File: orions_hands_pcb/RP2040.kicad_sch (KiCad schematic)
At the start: 25 parts, among them U1 RP2040, X1 ASE-12MHz

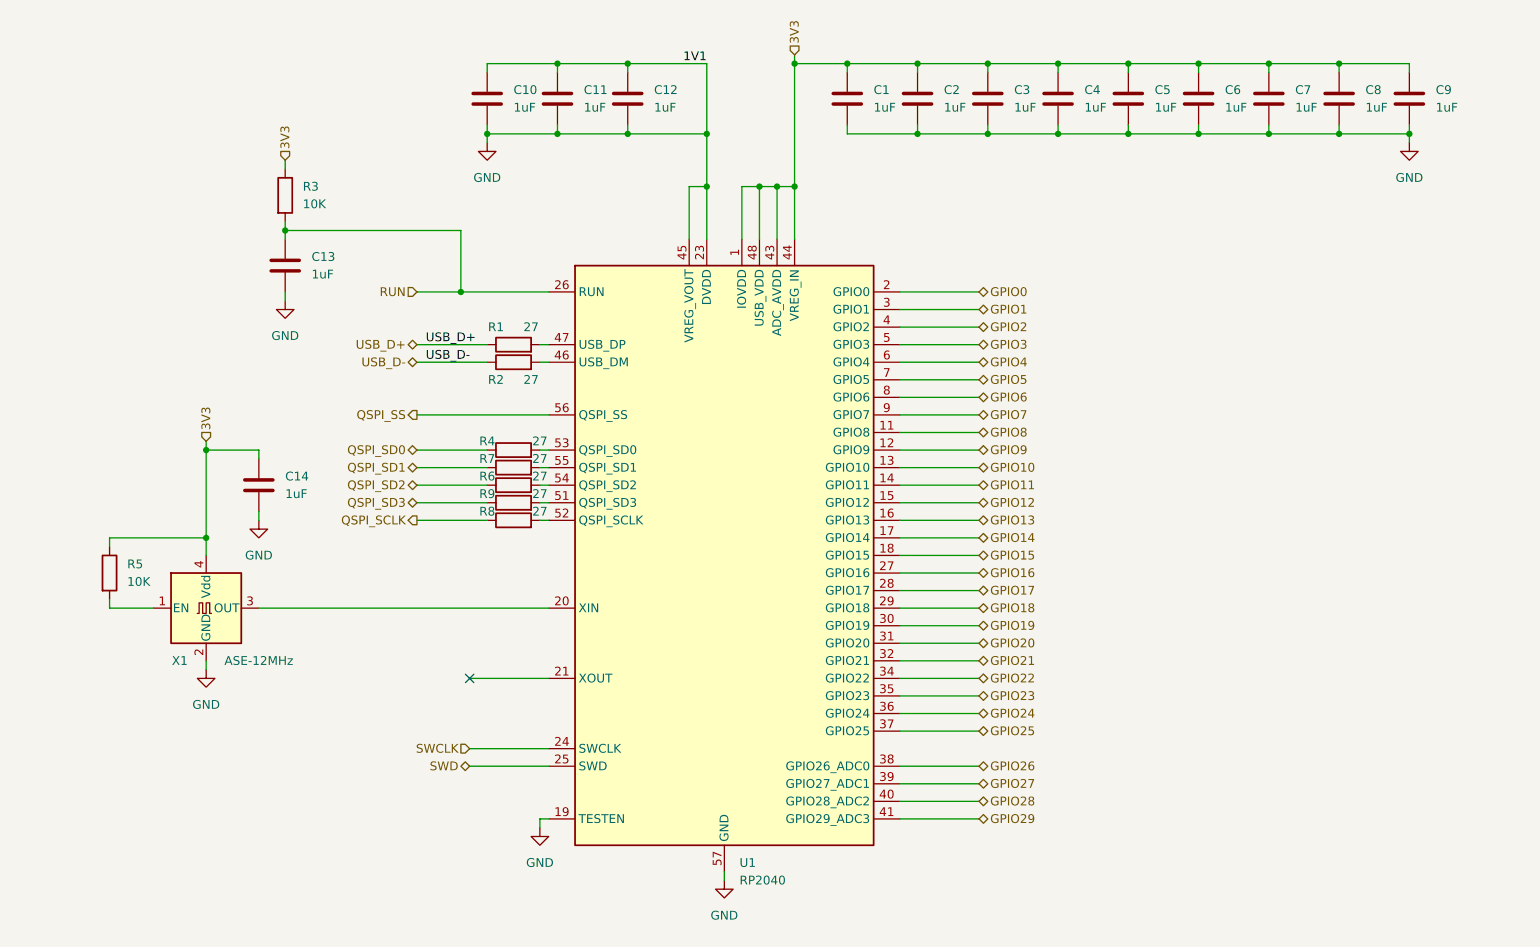
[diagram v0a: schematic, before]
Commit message: added power management + refined
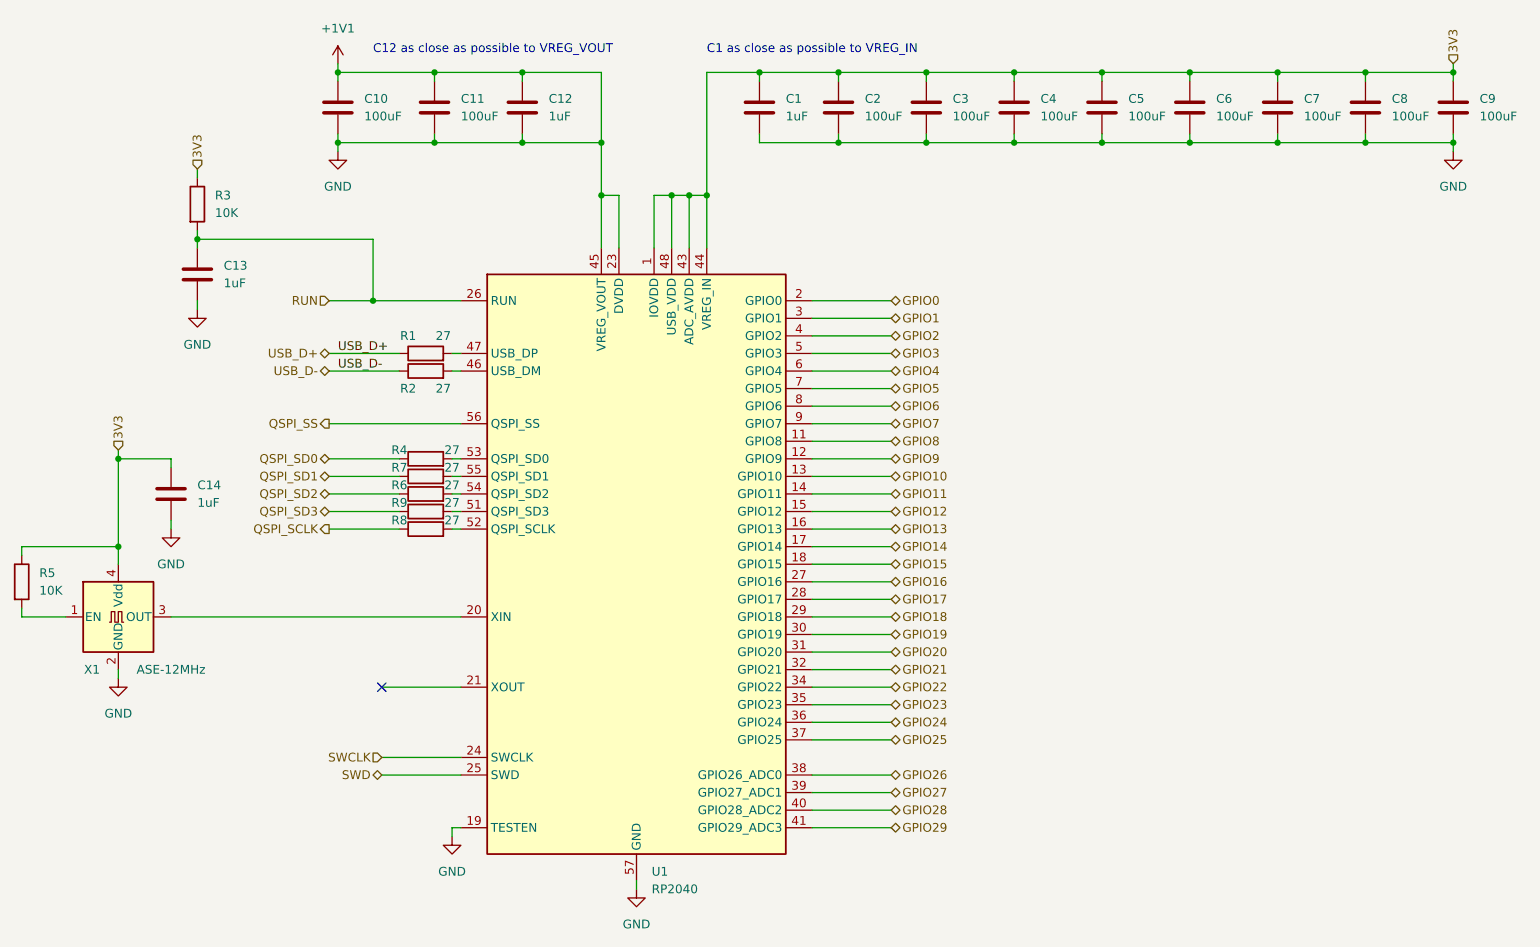
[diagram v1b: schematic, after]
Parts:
- C10, C11, C2, C3, C4, C5, C6, C7, C8, C9: value 1uF -> 100uF
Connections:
- net GND renamed +1V1
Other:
- note added: "C1 as close as possible to VREG_IN"
- note added: "C12 as close as possible to VREG_VOUT"
- moved on the sheet: C1, C10, C11, C12, C13, C14, C2, C3, C4, C5, C6, C7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

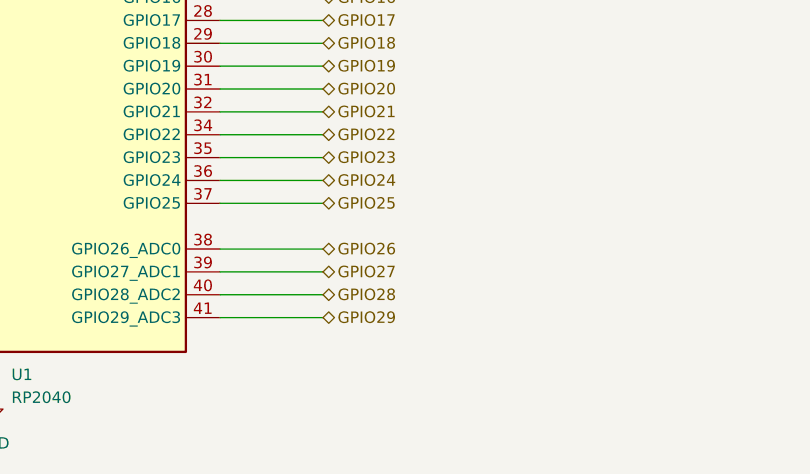
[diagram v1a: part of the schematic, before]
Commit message: SPI pin additions + gpio labeling
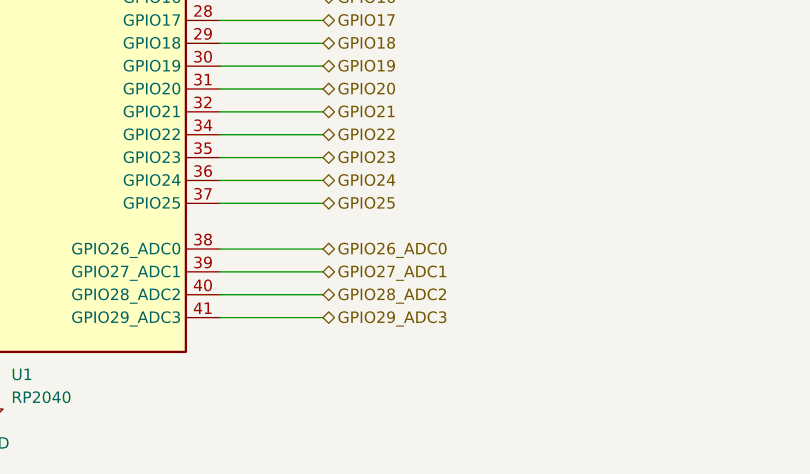
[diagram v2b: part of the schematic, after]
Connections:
- net GPIO26 renamed GPIO26_ADC0
- net GPIO27 renamed GPIO27_ADC1
- net GPIO28 renamed GPIO28_ADC2
- net GPIO29 renamed GPIO29_ADC3
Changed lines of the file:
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@@
     (effects (font (size 1.27 1.27)) (justify left))
   )
-  (hierarchical_label "GPIO29" (shape bidirectional) (at 176.53 144.78 0) (fields_autoplaced)
+  (hierarchical_label "GPIO29_ADC3" (shape bidirectional) (at 176.53 144.78 0) (fields_autoplaced)
     (effects (font (size 1.27 1.27)) (justify left))
   )
@@
     (effects (font (size 1.27 1.27)) (justify left))
   )
-  (hierarchical_label "GPIO28" (shape bidirectional) (at 176.53 142.24 0) (fields_autoplaced)
+  (hierarchical_label "GPIO28_ADC2" (shape bidirectional) (at 176.53 142.24 0) (fields_autoplaced)
     (effects (font (size 1.27 1.27)) (justify left))
   )
@@
     (effects (font (size 1.27 1.27)) (justify left))
   )
-  (hierarchical_label "GPIO27" (shape bidirectional) (at 176.53 139.7 0) (fields_autoplaced)
+  (hierarchical_label "GPIO27_ADC1" (shape bidirectional) (at 176.53 139.7 0) (fields_autoplaced)
     (effects (font (size 1.27 1.27)) (justify left))
   )
@@
     (effects (font (size 1.27 1.27)) (justify left))
   )
-  (hierarchical_label "GPIO26" (shape bidirectional) (at 176.53 137.16 0) (fields_autoplaced)
+  (hierarchical_label "GPIO26_ADC0" (shape bidirectional) (at 176.53 137.16 0) (fields_autoplaced)
     (effects (font (size 1.27 1.27)) (justify left))
   )
